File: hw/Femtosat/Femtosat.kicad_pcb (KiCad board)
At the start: 2 copper layers, 26 parts, among them J1 USB_B_Micro, J2 Programmer, J3 SMA, U0 AP7215-33YG-13, U1 SAMD21G, U2 TRH-G2, U3 XA1110, U4 RFM69HCW, Y1 32.768kHz

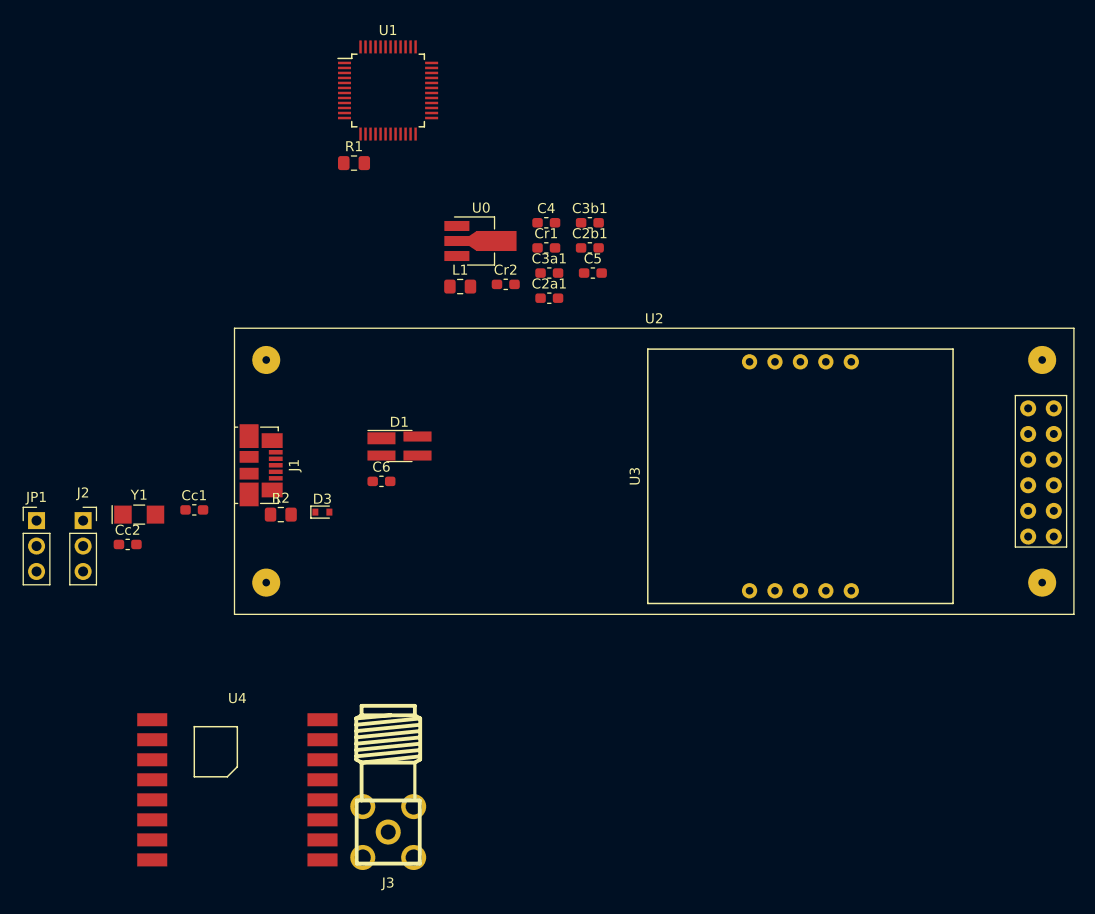
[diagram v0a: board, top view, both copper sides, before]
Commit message: Added capacitors for the communication system.
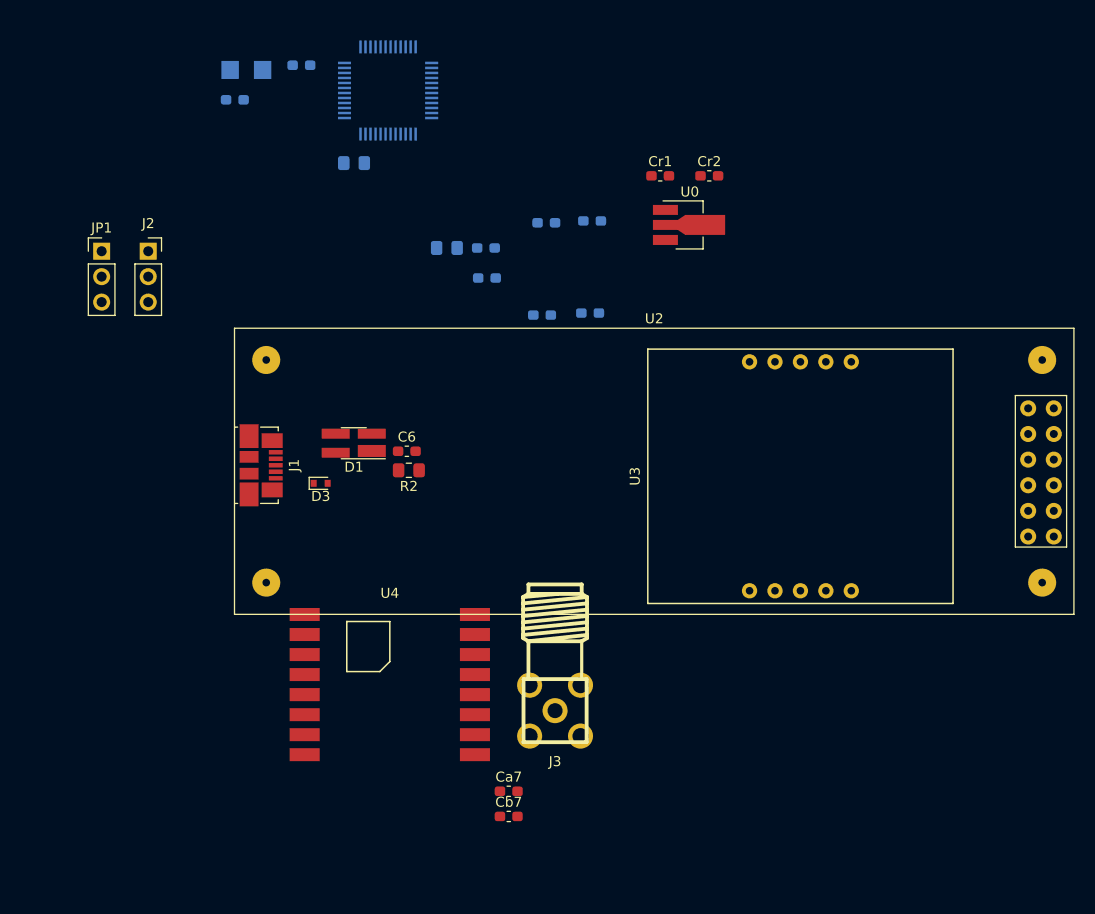
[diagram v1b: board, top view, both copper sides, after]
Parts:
- added Ca7: C, Capacitor_SMD:C_0603_1608Metric_Pad1.05x0.95mm_HandSolder, F.Cu at (128.6, 99.4)
- added Cb7: C, Capacitor_SMD:C_0603_1608Metric_Pad1.05x0.95mm_HandSolder, F.Cu at (128.6, 101.9)
- C2a1, C2b1, C3a1, C3b1, C4, C5, Cc1, Cc2, L1, R1, Y1: moved to B.Cu
- Ue: renamed from U1; moved to B.Cu
- moved Y1 45.7 mm to (102.4, 27.3)
- moved Cc1 45.7 mm to (107.9, 26.9)
- moved Cc2 45.7 mm to (101.2, 30.3)
- moved J2 27.7 mm to (92.6, 45.4)
- moved JP1 27.7 mm to (87.9, 45.4)
- moved Cr2 23.0 mm to (148.6, 37.9)
- moved U0 20.9 mm to (146.2, 42.8)
- moved J3 20.6 mm to (133.2, 91.3)
- moved U4 18.5 mm to (116.7, 88.7)
- moved R2 13.5 mm to (118.6, 67.3)
- moved Cr1 13.5 mm to (143.7, 37.9)
- moved C2b1 10.7 mm to (126.4, 48.1)
- moved C3b1 9.02 mm to (136.7, 51.6)
- moved C2a1 8.07 mm to (126.3, 45.1)
- moved C5 5.21 mm to (136.9, 42.4)
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
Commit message: Checking for the component's placement on the board.
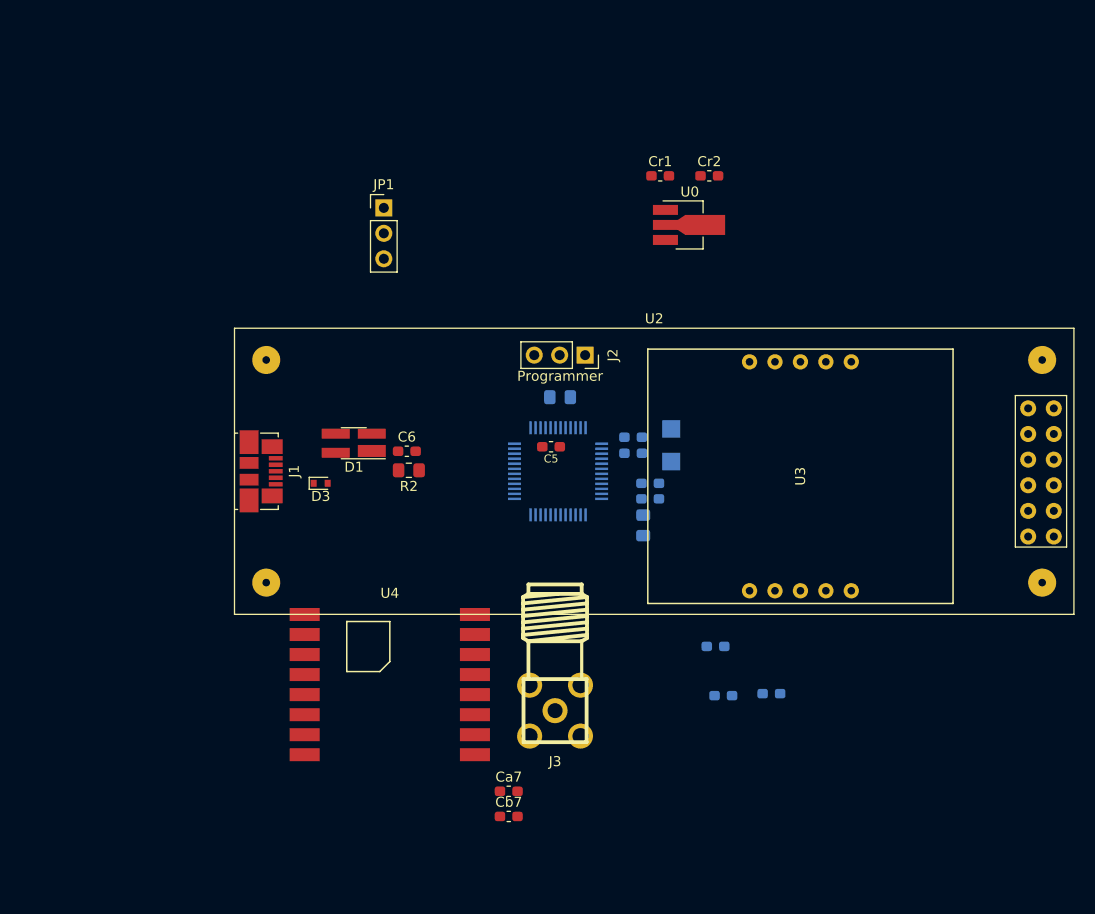
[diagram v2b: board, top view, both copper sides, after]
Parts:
- C5: moved to F.Cu
- moved Y1 56.6 mm to (144.8, 64.8), turned to 270 degrees
- moved Cc2 53.2 mm to (141.0, 65.6)
- moved Cc1 49.8 mm to (141.0, 64.0)
- moved C4 45.6 mm to (149.2, 84.9)
- moved J2 44.8 mm to (136.2, 55.8), turned to 270 degrees
- moved C3b1 42.1 mm to (154.8, 89.6)
- moved C3a1 42.1 mm to (150.0, 89.8)
- moved Ue 41.6 mm to (133.5, 67.4)
- moved L1 33.9 mm to (142.0, 72.8), turned to 270 degrees
- moved R1 31.1 mm to (133.7, 60.0)
- moved C2a1 28.7 mm to (142.7, 68.6)
- moved JP1 28.5 mm to (116.1, 41.1)
- moved C2b1 27.4 mm to (142.7, 70.2)
- moved C5 22.9 mm to (132.8, 65.0), turned to 180 degrees
- moved J1 0.60 mm to (103.8, 67.4)
